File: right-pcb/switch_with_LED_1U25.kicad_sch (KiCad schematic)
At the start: 4 parts, among them SW31 SW_SPST

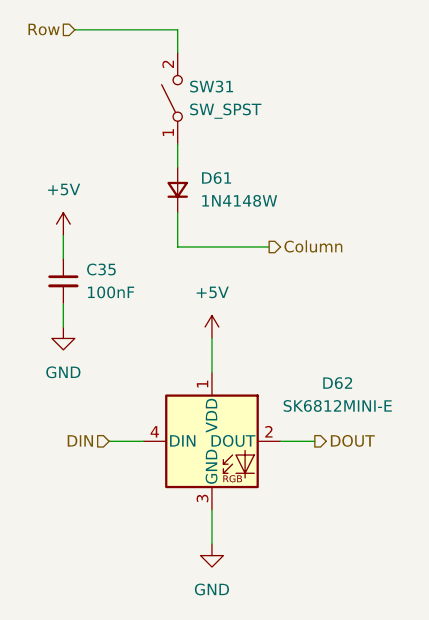
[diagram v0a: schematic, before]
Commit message: initial placement of switches and modifications from left to right
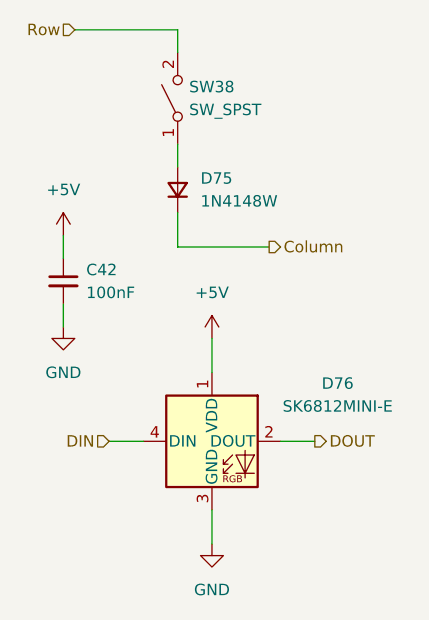
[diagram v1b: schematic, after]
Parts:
- renumbered C35 to C42, D61 to D75, D62 to D76, SW31 to SW38
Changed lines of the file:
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@@
 		(dnp no)
 		(fields_autoplaced yes)
-		(property "Reference" "#PWR0139"
+		(property "Reference" "#PWR0167"
 			(at 124.46 124.46 0)
 			(effects
@@
 				)
 				(path "/cf145565-22e2-4e5a-8a27-915862c57a1b/72dbedf5-0b03-4be1-b418-6a53323f317d"
-					(reference "#PWR064")
+					(reference "#PWR0175")
 					(unit 1)
 				)
 				(path "/cf145565-22e2-4e5a-8a27-915862c57a1b/74f1d740-4378-46c9-bc38-11c0ec54df6e"
-					(reference "#PWR0143")
+					(reference "#PWR0167")
 					(unit 1)
 				)
@@
 				)
 				(path "/cf145565-22e2-4e5a-8a27-915862c57a1b/c8cd9c33-6ded-45e7-a59e-413c0e5e412b"
-					(reference "#PWR0147")
+					(reference "#PWR0171")
 					(unit 1)
 				)
@@
 		(dnp no)
 		(fields_autoplaced yes)
-		(property "Reference" "D61"
+		(property "Reference" "D75"
 			(at 123.19 102.8699 90)
 			(effects
@@
 				)
 				(path "/cf145565-22e2-4e5a-8a27-915862c57a1b/72dbedf5-0b03-4be1-b418-6a53323f317d"
-					(reference "D55")
+					(reference "D79")
 					(unit 1)
 				)
 				(path "/cf145565-22e2-4e5a-8a27-915862c57a1b/74f1d740-4378-46c9-bc38-11c0ec54df6e"
-					(reference "D63")
+					(reference "D75")
 					(unit 1)
 				)
@@
 				)
 				(path "/cf145565-22e2-4e5a-8a27-915862c57a1b/c8cd9c33-6ded-45e7-a59e-413c0e5e412b"
-					(reference "D65")
+					(reference "D77")
 					(unit 1)
 				)
@@
 		(dnp no)
 		(fields_autoplaced yes)
-		(property "Reference" "D62"
+		(property "Reference" "D76"
 			(at 138.43 125.6598 0)
 			(effects
@@
 				)
 				(path "/cf145565-22e2-4e5a-8a27-915862c57a1b/72dbedf5-0b03-4be1-b418-6a53323f317d"
-					(reference "D56")
+					(reference "D80")
 					(unit 1)
 				)
 				(path "/cf145565-22e2-4e5a-8a27-915862c57a1b/74f1d740-4378-46c9-bc38-11c0ec54df6e"
-					(reference "D64")
+					(reference "D76")
 					(unit 1)
 				)
@@
 				)
 				(path "/cf145565-22e2-4e5a-8a27-915862c57a1b/c8cd9c33-6ded-45e7-a59e-413c0e5e412b"
-					(reference "D66")
+					(reference "D78")
 					(unit 1)
 				)
@@
 		(dnp no)
 		(fields_autoplaced yes)
-		(property "Reference" "#PWR0137"
+		(property "Reference" "#PWR0165"
 			(at 107.95 113.03 0)
 			(effects
@@
 		(instances
 			(project "row_staggered_split_keyboard_left_side"
+				(path "/cf145565-22e2-4e5a-8a27-915862c57a1b/72dbedf5-0b03-4be1-b418-6a53323f317d"
+					(reference "#PWR0173")
+					(unit 1)
+				)
 				(path "/cf145565-22e2-4e5a-8a27-915862c57a1b/74f1d740-4378-46c9-bc38-11c0ec54df6e"
-					(reference "#PWR0141")
+					(reference "#PWR0165")
 					(unit 1)
 				)
 				(path "/cf145565-22e2-4e5a-8a27-915862c57a1b/c8cd9c33-6ded-45e7-a59e-413c0e5e412b"
-					(reference "#PWR0145")
+					(reference "#PWR0169")
 					(unit 1)
 				)
@@
 		(dnp no)
 		(fields_autoplaced yes)
-		(property "Reference" "#PWR0140"
+		(property "Reference" "#PWR0168"
 			(at 124.46 149.86 0)
 			(effects
@@
 				)
 				(path "/cf145565-22e2-4e5a-8a27-915862c57a1b/72dbedf5-0b03-4be1-b418-6a53323f317d"
-					(reference "#PWR065")
+					(reference "#PWR0176")
 					(unit 1)
 				)
 				(path "/cf145565-22e2-4e5a-8a27-915862c57a1b/74f1d740-4378-46c9-bc38-11c0ec54df6e"
-					(reference "#PWR0144")
+					(reference "#PWR0168")
 					(unit 1)
 				)
@@
 				)
 				(path "/cf145565-22e2-4e5a-8a27-915862c57a1b/c8cd9c33-6ded-45e7-a59e-413c0e5e412b"
-					(reference "#PWR0148")
+					(reference "#PWR0172")
 					(unit 1)
 				)
@@
 		(dnp no)
 		(fields_autoplaced yes)
-		(property "Reference" "#PWR0138"
+		(property "Reference" "#PWR0166"
 			(at 107.95 125.73 0)
 			(effects
@@
 		(instances
 			(project "row_staggered_split_keyboard_left_side"
+				(path "/cf145565-22e2-4e5a-8a27-915862c57a1b/72dbedf5-0b03-4be1-b418-6a53323f317d"
+					(reference "#PWR0174")
+					(unit 1)
+				)
 				(path "/cf145565-22e2-4e5a-8a27-915862c57a1b/74f1d740-4378-46c9-bc38-11c0ec54df6e"
-					(reference "#PWR0142")
+					(reference "#PWR0166")
 					(unit 1)
 				)
 				(path "/cf145565-22e2-4e5a-8a27-915862c57a1b/c8cd9c33-6ded-45e7-a59e-413c0e5e412b"
-					(reference "#PWR0146")
+					(reference "#PWR0170")
 					(unit 1)
 				)
@@
 		(dnp no)
 		(fields_autoplaced yes)
-		(property "Reference" "SW31"
+		(property "Reference" "SW38"
 			(at 121.92 92.7099 90)
 			(effects
@@
 				)
 				(path "/cf145565-22e2-4e5a-8a27-915862c57a1b/72dbedf5-0b03-4be1-b418-6a53323f317d"
-					(reference "SW28")
+					(reference "SW40")
 					(unit 1)
 				)
 				(path "/cf145565-22e2-4e5a-8a27-915862c57a1b/74f1d740-4378-46c9-bc38-11c0ec54df6e"
-					(reference "SW32")
+					(reference "SW38")
 					(unit 1)
 				)
@@
 				)
 				(path "/cf145565-22e2-4e5a-8a27-915862c57a1b/c8cd9c33-6ded-45e7-a59e-413c0e5e412b"
-					(reference "SW33")
+					(reference "SW39")
 					(unit 1)
 				)
@@
 		(dnp no)
 		(fields_autoplaced yes)
-		(property "Reference" "C35"
+		(property "Reference" "C42"
 			(at 110.49 113.0362 0)
 			(effects
@@
 		(instances
 			(project "row_staggered_split_keyboard_left_side"
+				(path "/cf145565-22e2-4e5a-8a27-915862c57a1b/72dbedf5-0b03-4be1-b418-6a53323f317d"
+					(reference "C44")
+					(unit 1)
+				)
 				(path "/cf145565-22e2-4e5a-8a27-915862c57a1b/74f1d740-4378-46c9-bc38-11c0ec54df6e"
-					(reference "C36")
+					(reference "C42")
 					(unit 1)
 				)
 				(path "/cf145565-22e2-4e5a-8a27-915862c57a1b/c8cd9c33-6ded-45e7-a59e-413c0e5e412b"
-					(reference "C37")
-					(unit 1)
-				)
+					(reference "C43")
+					(unit 1)
+				)

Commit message: Boards were ordered
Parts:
- SW38: symbol Switch:SW_SPST -> SW-gElectroMech:SPST_MOM
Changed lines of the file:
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@@
 	)
 	(symbol
-		(lib_id "Switch:SW_SPST")
+		(lib_id "SW-gElectroMech:SPST_MOM")
 		(at 120.65 93.98 90)
 		(unit 1)
@@
 		)
 		(property "Datasheet" ""
-			(at 120.65 93.98 0)
+			(at 115.57 93.98 0)
 			(hide yes)
 			(show_name no)
@@
 			)
 		)
-		(property "Description" "Single Pole Single Throw (SPST) switch"
+		(property "Description" "Push button switch, generic, two pins"
 			(at 120.65 93.98 0)
 			(hide yes)
